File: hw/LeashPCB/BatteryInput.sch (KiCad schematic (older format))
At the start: 8 parts, among them J201 1020-1, J202 1020-1

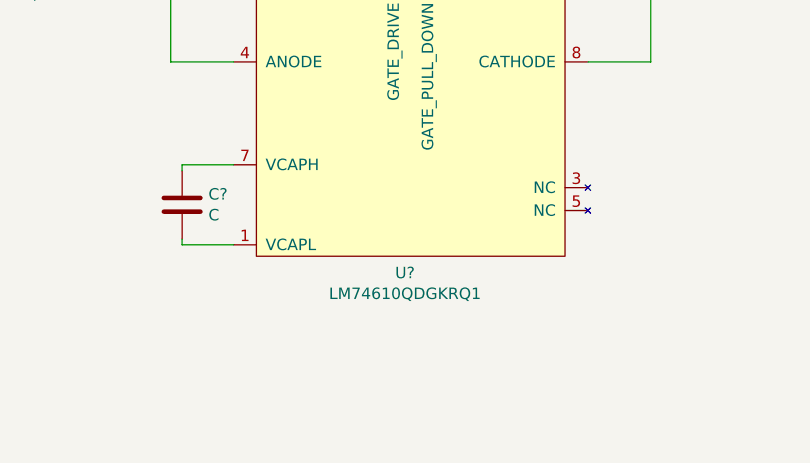
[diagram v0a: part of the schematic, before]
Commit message: Changed some file names to remove spaces and added circuits around the main power chips
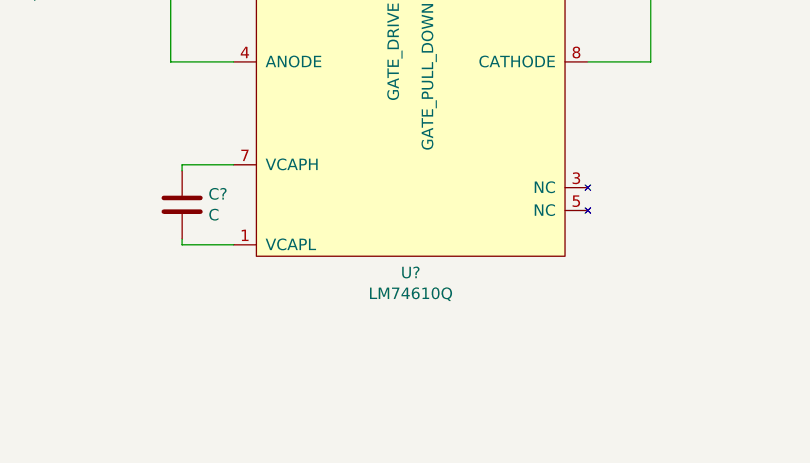
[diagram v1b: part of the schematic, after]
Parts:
- Q?: MPN1 (none) -> CSD18501Q5A; Standard Price (none) -> 0.16
- U?: value LM74610QDGKRQ1 -> LM74610Q; Link1 (none) -> http://www.ti.com/product/LM74610-Q1; MPN1 (none) -> LM74610QDGKRQ1; Standard Price (none) -> 0.23; Vendor1 (none) -> Texas Instruments
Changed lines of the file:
@@
 U 1 1 5D069D70
 P 7150 3400
-F 0 "U?" H 7050 2727 50  0000 C CNN
-F 1 "LM74610QDGKRQ1" H 7050 2636 50  0000 C CNN
+F 0 "U?" H 7075 2727 50  0000 C CNN
+F 1 "LM74610Q" H 7075 2636 50  0000 C CNN
 F 2 "" H 6400 3100 50  0001 C CNN
-F 3 "" H 6400 3100 50  0001 C CNN
+F 3 "http://www.ti.com/lit/ds/symlink/lm74610-q1.pdf" H 6400 3100 50  0001 C CNN
+F 4 "LM74610QDGKRQ1" H 7150 3400 50  0001 C CNN "MPN1"
+F 5 "http://www.ti.com/product/LM74610-Q1" H 7150 3400 50  0001 C CNN "Link1"
+F 6 "Texas Instruments" H 7150 3400 50  0001 C CNN "Vendor1"
+F 7 "0.23" H 7150 3400 50  0001 C CNN "Standard Price"
 	1    7150 3400
 	1    0    0    -1
@@
 F 2 "Package_TO_SOT_SMD:TDSON-8-1" H 7200 2075 50  0001 L CIN
 F 3 "http://www.ti.com/lit/gpn/csd18501q5a" V 7000 2150 50  0001 L CNN
+F 4 "0.16" H 7000 2150 50  0001 C CNN "Standard Price"
+F 5 "CSD18501Q5A" H 7000 2150 50  0001 C CNN "MPN1"
 	1    7000 2150
 	0    1    -1   0

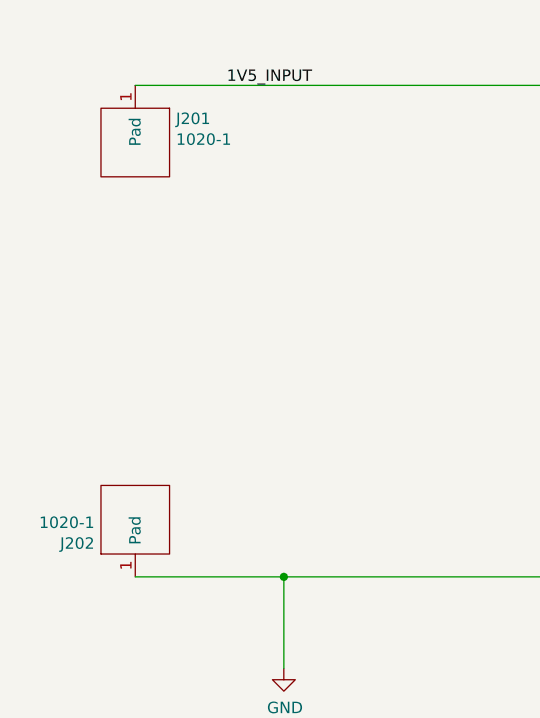
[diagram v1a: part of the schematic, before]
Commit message: Changed around configuration of some parts and added top level cost estimates to block diagram
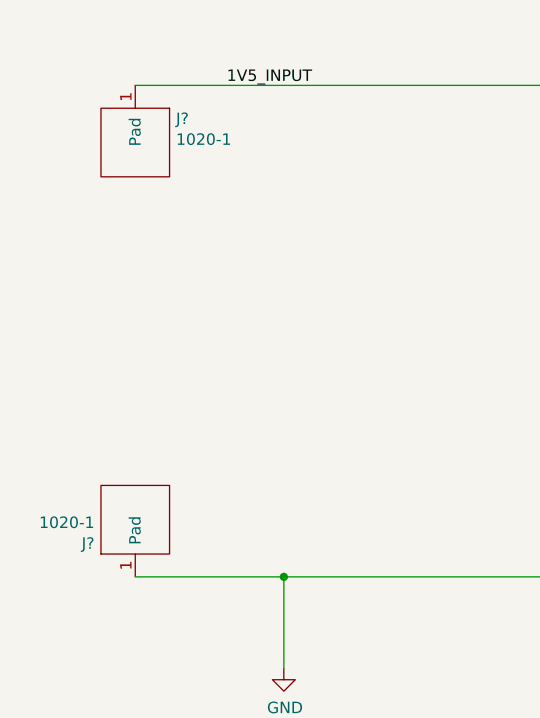
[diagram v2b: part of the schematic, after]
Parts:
- J?: renamed from J202; Standard Price 0.15 -> 0.05
- J?: renamed from J201; Standard Price 0.15 -> 0.05
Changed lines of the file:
@@
 EESchema Schematic File Version 4
-LIBS:LeashPCB-cache
 EELAYER 29 0
 EELAYER END
@@
 	3300 4200 3300 4600
 $Comp
-L power:GND #PWR0201
+L power:GND #PWR?
 U 1 1 5D079C2D
 P 3300 4600
-F 0 "#PWR0201" H 3300 4350 50  0001 C CNN
+F 0 "#PWR?" H 3300 4350 50  0001 C CNN
 F 1 "GND" H 3305 4427 50  0000 C CNN
 F 2 "" H 3300 4600 50  0001 C CNN
@@
 	2650 4200 3300 4200
 $Comp
-L LeashPCB:1020-1 J202
+L LeashPCB:1020-1 J?
 U 1 1 5D079C36
 P 2650 4000
-F 0 "J202" V 2596 4178 50  0000 L CNN
+F 0 "J?" V 2596 4178 50  0000 L CNN
 F 1 "1020-1" V 2687 4178 50  0000 L CNN
 F 2 "leash:1020-1" H 2650 4000 50  0001 C CNN
 F 3 "" H 2650 4000 50  0001 C CNN
-F 4 "0.15" H 2650 4000 50  0001 C CNN "Standard Price"
+F 4 "0.05" H 2650 4000 50  0001 C CNN "Standard Price"
 	1    2650 4000
 	0    -1   -1   0
@@
 $EndBitmap
 $Comp
-L LeashPCB:1020-1 J201
+L LeashPCB:1020-1 J?
 U 1 1 5D079C5E
 P 2650 2250
-F 0 "J201" V 2596 2428 50  0000 L CNN
+F 0 "J?" V 2596 2428 50  0000 L CNN
 F 1 "1020-1" V 2687 2428 50  0000 L CNN
 F 2 "leash:1020-1" H 2650 2250 50  0001 C CNN
 F 3 "" H 2650 2250 50  0001 C CNN
-F 4 "0.15" H 2650 2250 50  0001 C CNN "Standard Price"
+F 4 "0.05" H 2650 2250 50  0001 C CNN "Standard Price"
 	1    2650 2250
 	0    1    1    0

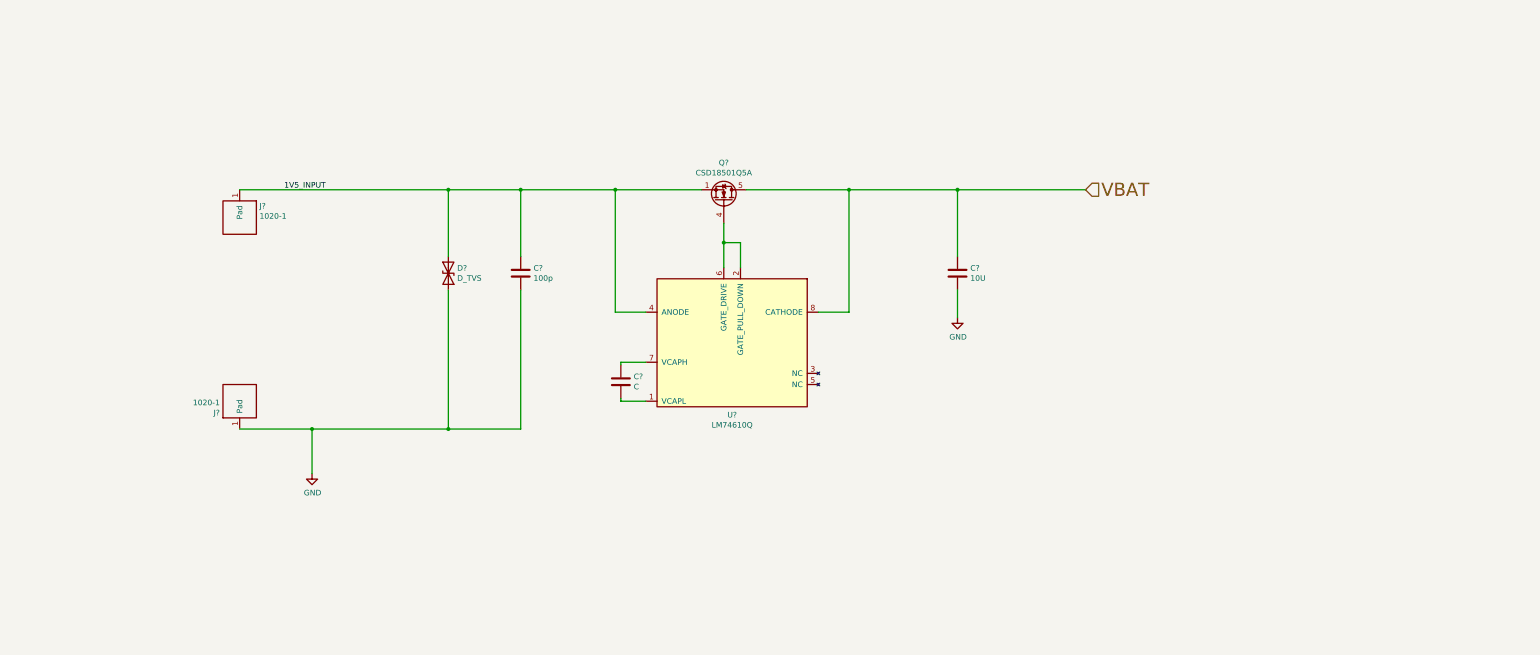
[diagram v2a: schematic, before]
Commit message: Swapped out second boost for a buck. Will now take all inputs up to 5V and then buck down to 3v3 for processor
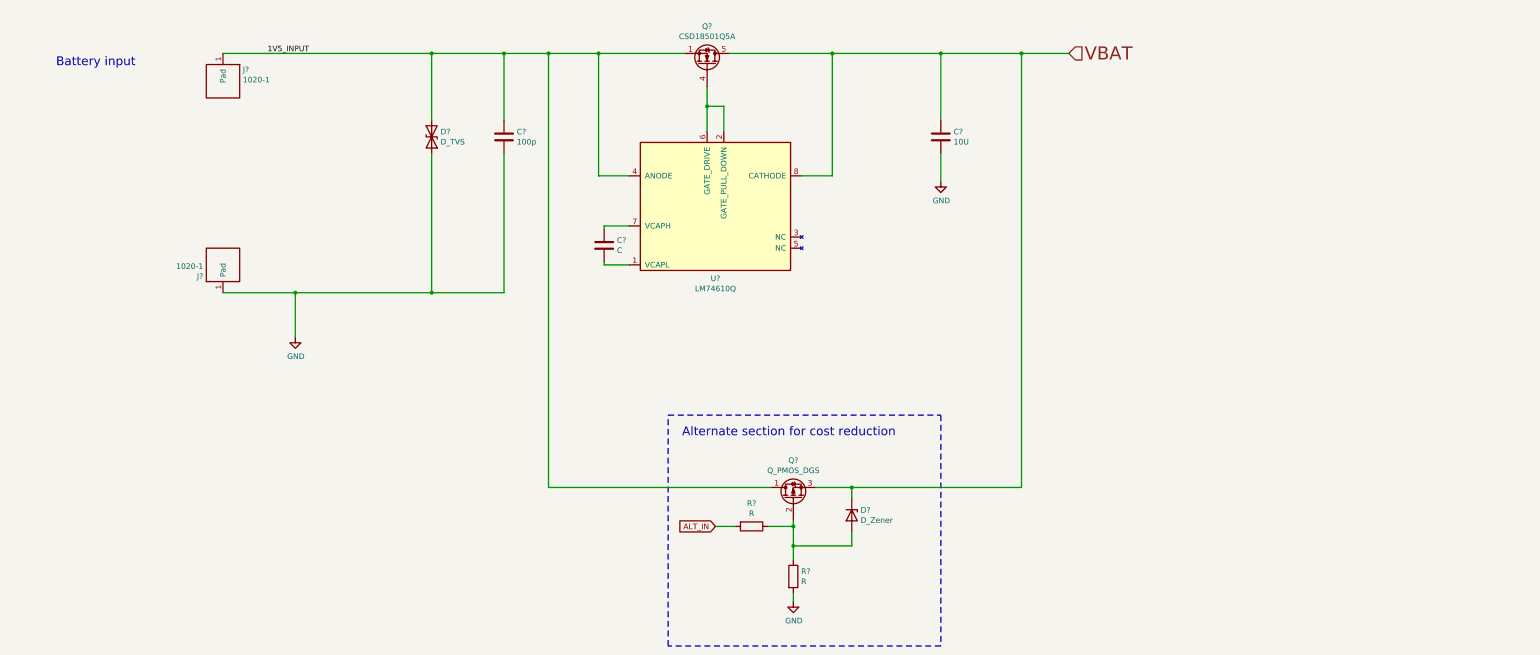
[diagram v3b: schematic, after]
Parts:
- added D?: D_Zener, symbol Device:D_Zener
- added Q?: Q_PMOS_DGS, symbol Device:Q_PMOS_DGS
- added R? (x2): R, symbol Device:R
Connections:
- net 1V5_INPUT: now also Q?.1 (D)
- net GND: now also R?.2
- net VBAT: now also D?.1 (K), Q?.3 (S)
- new net: D?.2 (A), Q?.2 (G), R?.1, R?.1
- new net ALT_IN: R?.2
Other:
- note added: "Alternate section for cost reduction"
- note added: "Battery input"
- moved on the sheet: C?, D?, J?, Q?, U?

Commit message: Added more top level signals to block diagram and added alternate population options for power
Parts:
- added J?: Conn_01x03, symbol Connector_Generic:Conn_01x03
- added R?: 0, symbol Device:R
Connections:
- wire segments 45 -> 56
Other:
- note added: "Jumper section to switch\nbetween battery and ALT"
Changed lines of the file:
@@
 EELAYER 29 0
 EELAYER END
-$Descr A4 11693 8268
+$Descr B 17000 11000
 encoding utf-8
 Sheet 2 10
@@
 	0    1    1    0
 $EndComp
-Text HLabel 10100 825  2    118  Input ~ 0
+Text HLabel 13500 825  2    118  Input ~ 0
 VBAT
 Text Label 2900 825  0    50   ~ 0
@@
 Wire Wire Line
 	5875 825  5425 825
-Text Notes 1000 950  0    79   ~ 0
+Text Notes 3350 1750 0    79   ~ 0
 Battery input
 Wire Wire Line
@@
 	8150 4725 9675 4725
 Connection ~ 9675 825
-Wire Wire Line
-	9675 825  10100 825
 Wire Notes Line
 	6500 4075 8950 4075
@@
 Text Notes 6625 4275 0    79   ~ 0
 Alternate section for cost reduction
+$Comp
+L Device:R R?
+U 1 1 5D1B1ECE
+P 11250 825
+F 0 "R?" V 11043 825 50  0000 C CNN
+F 1 "0" V 11134 825 50  0000 C CNN
+F 2 "" V 11180 825 50  0001 C CNN
+F 3 "~" H 11250 825 50  0001 C CNN
+	1    11250 825
+	0    1    1    0
+$EndComp
+Wire Wire Line
+	9675 825  10025 825
+Wire Wire Line
+	11400 825  12675 825
+Wire Wire Line
+	10000 2425 10025 825
+Connection ~ 10025 825
+Wire Wire Line
+	10025 825  11100 825
+Text GLabel 11800 2200 2    50   Input ~ 0
+ALT_IN
+Wire Wire Line
+	12675 2500 12675 825
+Connection ~ 12675 825
+Wire Wire Line
+	12675 825  13500 825
+Wire Notes Line
+	10125 1150 12575 1150
+Wire Notes Line
+	12575 1150 12575 3225
+Text Notes 10250 1350 0    79   ~ 0
+Alternate section for cost reduction
+Wire Notes Line
+	12575 3225 10125 3225
+Wire Notes Line
+	10125 1150 10125 3225
+$Comp
+L Connector_Generic:Conn_01x03 J?
+U 1 1 5D1CF8AA
+P 11300 1850
+F 0 "J?" V 11264 1662 50  0000 R CNN
+F 1 "Conn_01x03" V 11173 1662 50  0000 R CNN
+F 2 "" H 11300 1850 50  0001 C CNN
+F 3 "~" H 11300 1850 50  0001 C CNN
+	1    11300 1850
+	0    -1   -1   0
+$EndComp
+Wire Wire Line
+	11400 2050 11400 2200
+Wire Wire Line
+	11400 2200 11800 2200
+Wire Wire Line
+	11300 2050 11300 2500
+Wire Wire Line
+	11200 2425 11200 2050
+Wire Wire Line
+	10000 2425 11200 2425
+Wire Wire Line
+	11300 2500 12675 2500
+Text Notes 10875 2750 0    50   ~ 0
+Jumper section to switch\nbetween battery and ALT
 $EndSCHEMATC

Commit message: Added multiple configurations for test board
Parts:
- removed J?: Conn_01x03, symbol Connector_Generic:Conn_01x03
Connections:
- net labels added: V_BAT
- net labels removed: VBAT
- wire segments 56 -> 46
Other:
- note added: "Maybe consider making the \npositive side to be Keystone 55TR?"
- note removed: "Jumper section to switch\nbetween battery and ALT"
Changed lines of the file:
@@
 EESchema Schematic File Version 4
 LIBS:LeashPCB-cache
-LIBS:TVRTN-cache
 EELAYER 29 0
 EELAYER END
@@
 	0    1    1    0
 $EndComp
-Text HLabel 13500 825  2    118  Input ~ 0
-VBAT
+Text HLabel 13500 825  2    118  Output ~ 0
+V_BAT
 Text Label 2900 825  0    50   ~ 0
 1V5_INPUT
@@
 $EndComp
 Wire Wire Line
-	9675 825  10025 825
-Wire Wire Line
-	11400 825  12675 825
-Wire Wire Line
-	10000 2425 10025 825
-Connection ~ 10025 825
-Wire Wire Line
-	10025 825  11100 825
-Text GLabel 11800 2200 2    50   Input ~ 0
-ALT_IN
-Wire Wire Line
-	12675 2500 12675 825
-Connection ~ 12675 825
-Wire Wire Line
-	12675 825  13500 825
-Wire Notes Line
-	10125 1150 12575 1150
-Wire Notes Line
-	12575 1150 12575 3225
-Text Notes 10250 1350 0    79   ~ 0
-Alternate section for cost reduction
-Wire Notes Line
-	12575 3225 10125 3225
-Wire Notes Line
-	10125 1150 10125 3225
-$Comp
-L Connector_Generic:Conn_01x03 J?
-U 1 1 5D1CF8AA
-P 11300 1850
-F 0 "J?" V 11264 1662 50  0000 R CNN
-F 1 "Conn_01x03" V 11173 1662 50  0000 R CNN
-F 2 "" H 11300 1850 50  0001 C CNN
-F 3 "~" H 11300 1850 50  0001 C CNN
-	1    11300 1850
-	0    -1   -1   0
-$EndComp
-Wire Wire Line
-	11400 2050 11400 2200
-Wire Wire Line
-	11400 2200 11800 2200
-Wire Wire Line
-	11300 2050 11300 2500
-Wire Wire Line
-	11200 2425 11200 2050
-Wire Wire Line
-	10000 2425 11200 2425
-Wire Wire Line
-	11300 2500 12675 2500
-Text Notes 10875 2750 0    50   ~ 0
-Jumper section to switch\nbetween battery and ALT
+	9675 825  11100 825
+Wire Wire Line
+	11400 825  13500 825
+Text Notes 575  750  0    98   ~ 0
+Maybe consider making the \npositive side to be Keystone 55TR?
 $EndSCHEMATC
